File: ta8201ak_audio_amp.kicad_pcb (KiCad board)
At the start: 2 copper layers, 42.3 x 35.4 mm, 20 parts, among them J1 Conn_01x01_Pin, J2 Conn_01x01_Pin, J3 Conn_01x01_Pin, J4 Conn_01x01_Pin, J5 Conn_01x01_Pin, U1 TA8201AK

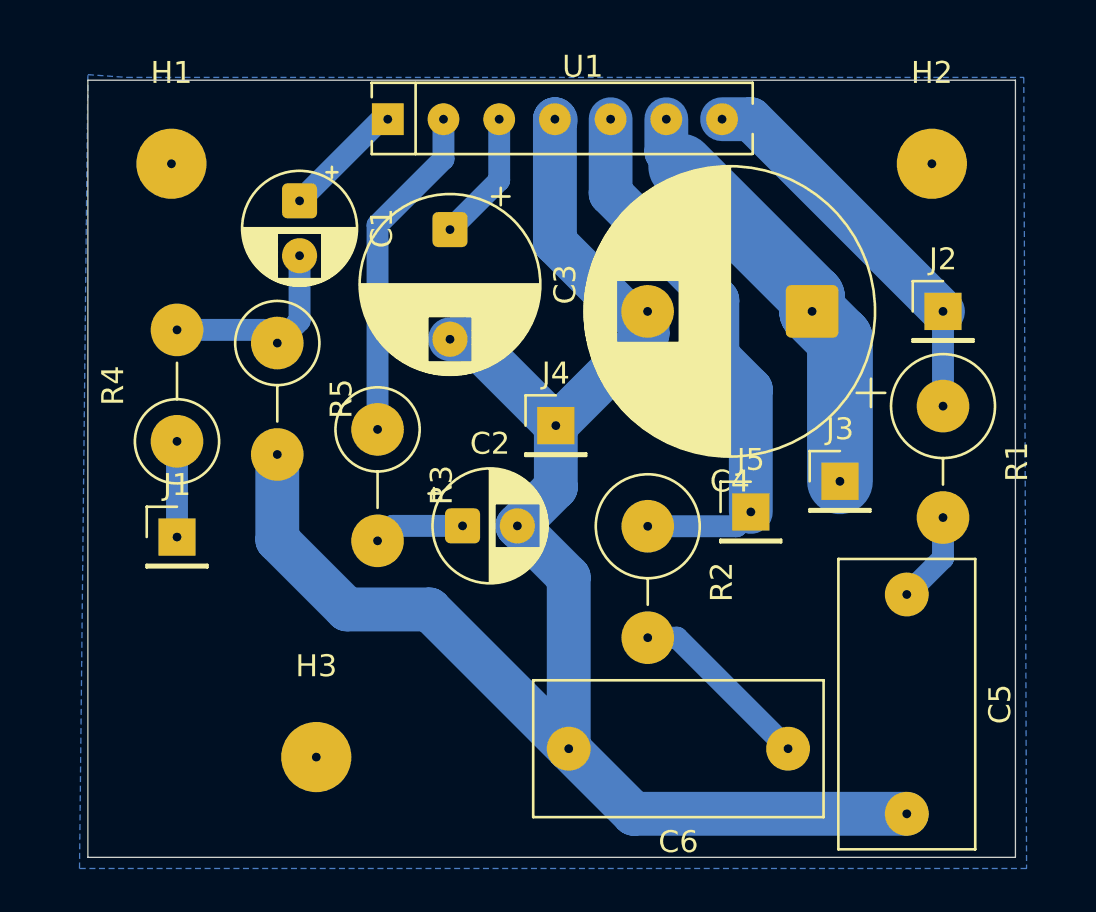
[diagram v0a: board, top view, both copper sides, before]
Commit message: 配置と配線を修正
配線の修正
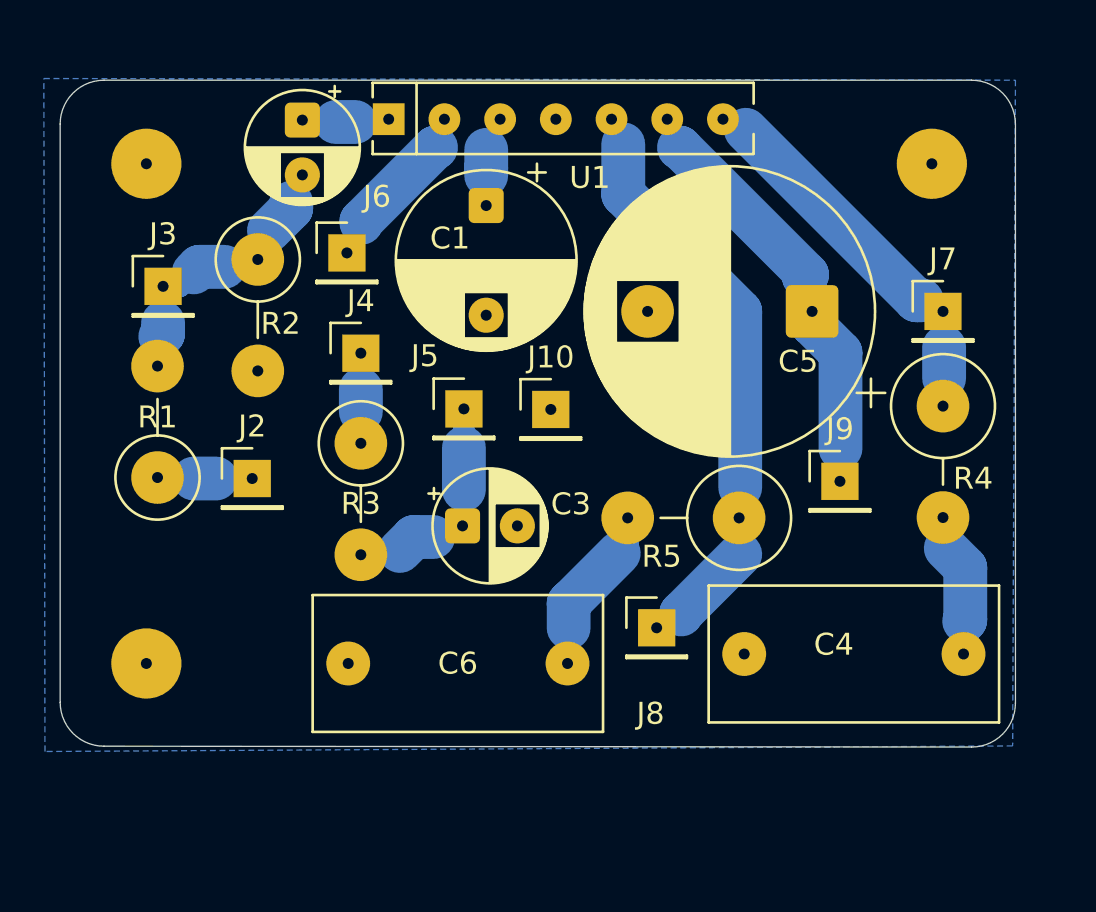
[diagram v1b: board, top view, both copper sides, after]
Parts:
- removed J1: Conn_01x01_Pin, Connector_PinHeader_2.54mm:PinHeader_1x01_P2.54mm_Vertical
- removed the R1 at (189.7, 68.1)
- added J2: SW1_1, Connector_PinHeader_2.54mm:PinHeader_1x01_P2.54mm_Vertical, F.Cu at (158.2, 71.4)
- added J3: SW1_2, Connector_PinHeader_2.54mm:PinHeader_1x01_P2.54mm_Vertical, F.Cu at (154.2, 62.6)
- added J4: SW2_2, Connector_PinHeader_2.54mm:PinHeader_1x01_P2.54mm_Vertical, F.Cu at (163.2, 65.7)
- added J5: SW2_3, Connector_PinHeader_2.54mm:PinHeader_1x01_P2.54mm_Vertical, F.Cu at (167.9, 68.2)
- added J6: SW2_1, Connector_PinHeader_2.54mm:PinHeader_1x01_P2.54mm_Vertical, F.Cu at (162.6, 61.1)
- added R4: 2.2, Resistor_THT:R_Axial_DIN0414_L11.9mm_D4.5mm_P5.08mm_Vertical, F.Cu at (189.7, 68.1)
- C1: renamed from C3; value 220uF -> 220u
- C3: renamed from C2; value 47uF -> 47u
- C4: renamed from C5; value 0.15uF -> 0.15u
- C6: value 0.15uF -> 0.15u
- J10: renamed from J4; value Conn_01x01_Pin -> Gnd
- J7: renamed from J2; value Conn_01x01_Pin -> Out1
- J8: renamed from J5; value Conn_01x01_Pin -> Out2
- J9: renamed from J3; value Conn_01x01_Pin -> Vcc
- R1: renamed from R4; value 39kΩ -> 39k
- R2: renamed from R5; value 10kΩ -> 10k
- U1: value TA8201AK -> ~
- moved C6 10.8 mm to (172.6, 79.8)
- moved H3 8.84 mm to (153.4, 79.8)
- moved J8 6.81 mm to (176.7, 78.2)
- moved R5 4.18 mm to (180.4, 73.2), turned to 180 degrees
- moved R2 3.91 mm to (158.5, 61.4)
- moved C4 3.75 mm to (190.7, 79.4), turned to 180 degrees
- moved C2 3.69 mm to (160.5, 55.0)
- moved C1 1.98 mm to (168.9, 58.9)
- moved R1 1.88 mm to (153.9, 71.3)
- moved H1 1.14 mm to (153.4, 57.0)
- moved R3 0.99 mm to (163.2, 69.8)
- moved J10 0.77 mm to (171.9, 68.2)
- renumbered C1 to C2, C4 to C5, R2 to R5
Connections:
- R3 pad 1: Net-(U1-NF) -> Net-(J4-Pin_1)
- U1 pad 2: Net-(U1-NF) -> Net-(J6-Pin_1)
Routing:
- net GND: track 78.8 -> 0.00 mm
- net Net-(U1-NF): track 15.4 -> 0.00 mm
- net Net-(J6-Pin_1): track 0.00 -> 4.87 mm
- net Net-(U1-R.F): track 5.96 -> 1.17 mm
- net Net-(J7-Pin_1): track 18.0 -> 14.1 mm
- net Net-(J5-Pin_1): track 4.16 -> 7.36 mm
- net Net-(U1-IN): track 5.56 -> 2.45 mm
- net VCC: track 19.8 -> 16.9 mm
- net Net-(C4-Pad1): track 4.19 -> 6.68 mm
- net Net-(J4-Pin_1): track 0.00 -> 2.46 mm
- net Net-(J2-Pin_1): track 4.36 -> 2.69 mm
- net Net-(J3-Pin_1): track 9.22 -> 8.47 mm
- net Net-(C6-Pad1): track 8.49 -> 7.77 mm
- net Net-(J8-Pin_1): track 25.5 -> 25.0 mm
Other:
- board size 42.3 x 35.4 mm -> 43.6 x 30.4 mm

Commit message: 仕切り直す
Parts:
- removed the J2 at (158.2, 71.4)
- removed the J3 at (154.2, 62.6)
- removed the J4 at (163.2, 65.7)
- removed the J5 at (167.9, 68.2)
- removed J6: SW2_1, Connector_PinHeader_2.54mm:PinHeader_1x01_P2.54mm_Vertical
- added J1: IN, Connector_PinHeader_2.54mm:PinHeader_1x01_P2.54mm_Vertical, F.Cu at (158.5, 71.4)
- C2: renamed from C3; value 47u -> 47uF
- C3: renamed from C1; value 220u -> 220uF
- C5: renamed from C4; value 0.15u -> 0.15uF
- C6: value 0.15u -> 0.15uF
- R4: renamed from R1; value 39k -> 39kΩ
- R5: renamed from R2; value 10k -> 10kΩ
- renumbered C2 to C1, C5 to C4, J7 to J2, J9 to J3, J10 to J4, J8 to J5, R4 to R1, R5 to R2
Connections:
- R3 pad 1: Net-(J4-Pin_1) -> Net-(U1-NF)
- U1 pad 2: Net-(J6-Pin_1) -> Net-(U1-NF)
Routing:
- net Net-(U1-NF): track 0.00 -> 14.9 mm
- net Net-(J6-Pin_1): track 4.87 -> 0.00 mm
- net Net-(C2-Pad1): track 7.36 -> 3.67 mm
- net Net-(J4-Pin_1): track 2.46 -> 0.00 mm

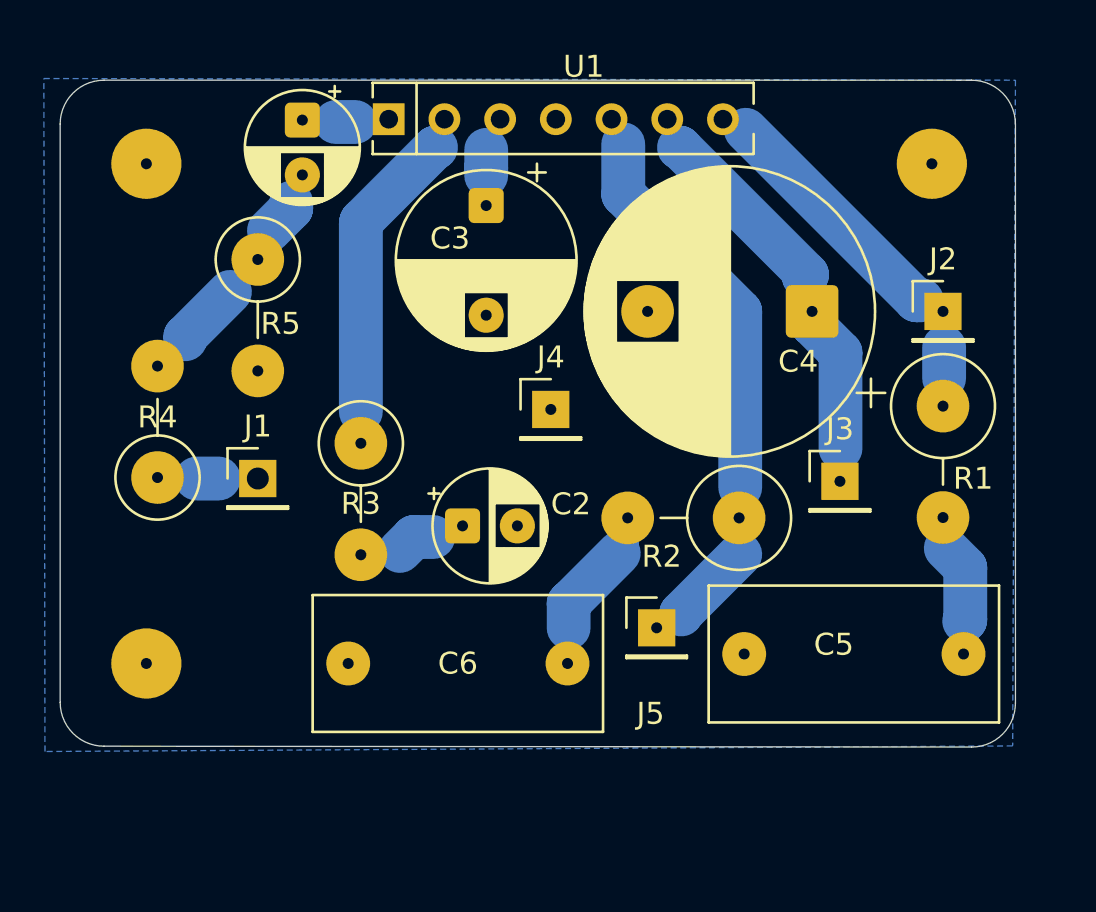
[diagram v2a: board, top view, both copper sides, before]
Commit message: エレキギター向けに抵抗やコンデンサを変更
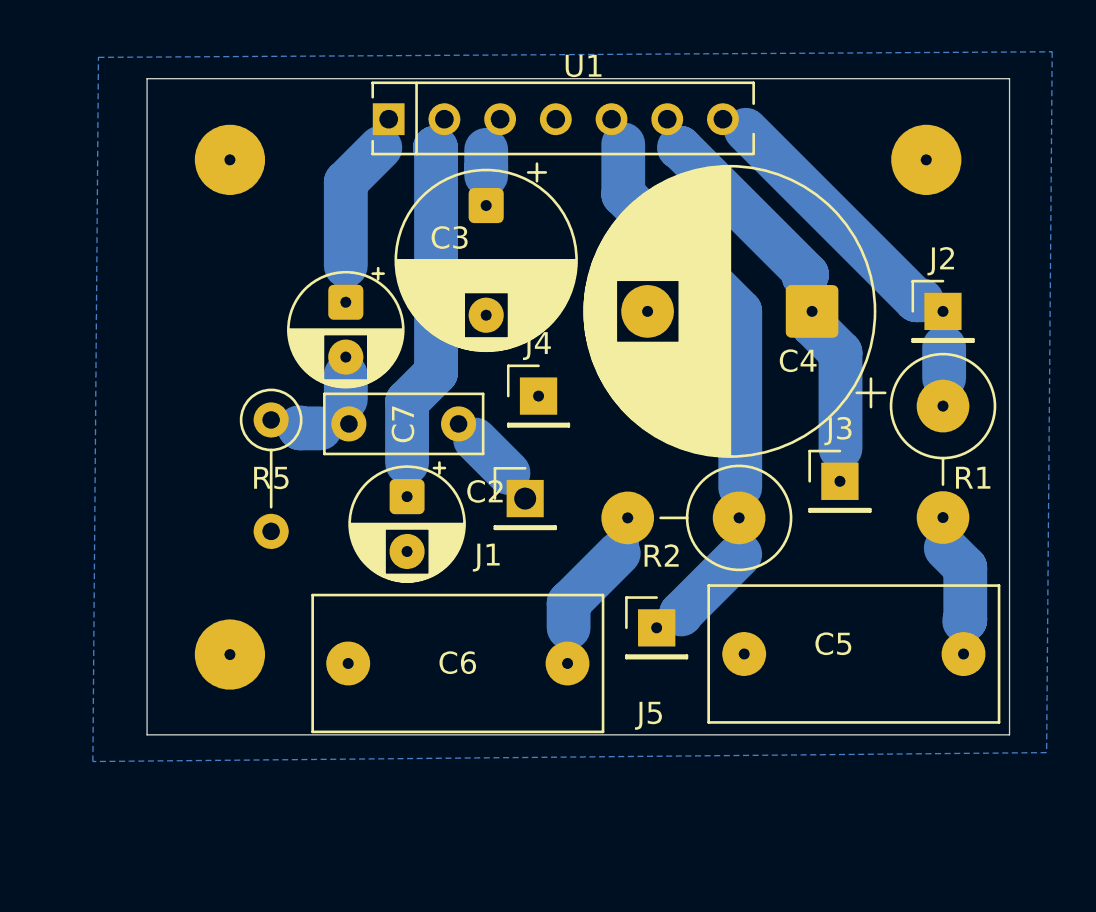
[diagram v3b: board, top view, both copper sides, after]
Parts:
- removed R3: 620, Resistor_THT:R_Axial_DIN0411_L9.9mm_D3.6mm_P5.08mm_Vertical
- removed R4: 39kΩ, Resistor_THT:R_Axial_DIN0411_L9.9mm_D3.6mm_P5.08mm_Vertical
- added C7: 0.022u, Capacitor_THT:C_Rect_L7.0mm_W2.5mm_P5.00mm, F.Cu at (167.7, 68.9)
- C1: value 4.7uF -> 4.7u
- C2: value 47uF -> 47u
- C3: value 220uF -> 220u
- C4: value 1000uF -> 1000u
- C5, C6: value 0.15uF -> 0.15u
- R5: value 10kΩ -> 1M; footprint Resistor_THT:R_Axial_DIN0411_L9.9mm_D3.6mm_P5.08mm_Vertical -> Resistor_THT:R_Axial_DIN0207_L6.3mm_D2.5mm_P5.08mm_Vertical
- moved J1 12.2 mm to (170.7, 72.3)
- moved C1 8.54 mm to (162.5, 63.3)
- moved R5 7.34 mm to (159.1, 68.7)
- moved H3 3.83 mm to (157.2, 79.4)
- moved H1 3.81 mm to (157.2, 56.8)
- moved C2 2.86 mm to (165.3, 72.2), turned to -90 degrees
- moved J4 0.83 mm to (171.3, 67.6)
- moved H2 0.31 mm to (189.0, 56.8)
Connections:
- C2 pad 1: Net-(C2-Pad1) -> Net-(U1-NF)
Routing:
- net Net-(U1-IN): track 2.45 -> 7.70 mm
- net Net-(C1-Pad2): track 7.99 -> 2.97 mm
- net Net-(C2-Pad1): track 3.67 -> 0.00 mm
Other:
- board size 43.6 x 30.4 mm -> 39.3 x 29.9 mm

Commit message: 利得制限の抵抗は外した アッテネーターの合成抵抗をエレキギター向けに1Mに近づけた 高音補正用のセラミックコンデンサとボリュームを追加
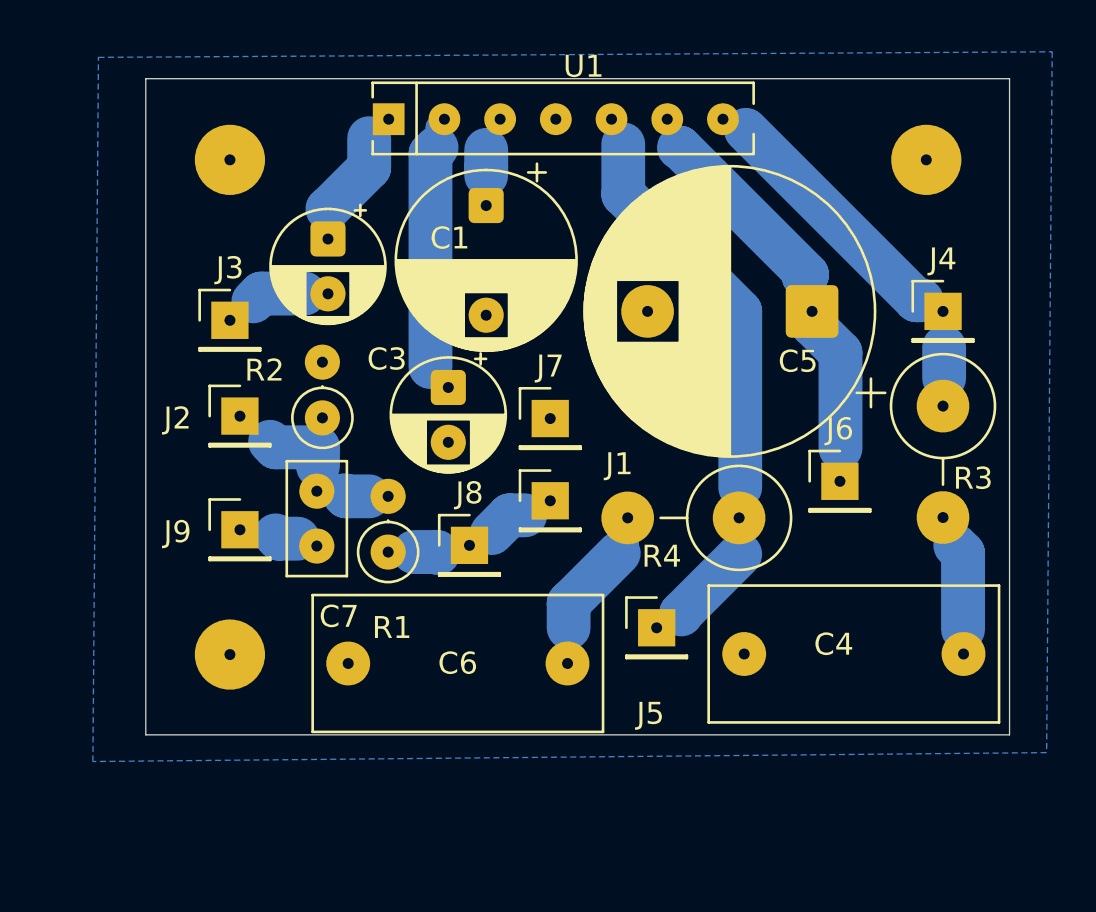
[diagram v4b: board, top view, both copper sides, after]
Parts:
- removed the C2 at (165.3, 72.2)
- added C3: 47u, Capacitor_THT:CP_Radial_D5.0mm_P2.50mm, F.Cu at (167.2, 67.2)
- added J2: RV1_3, Connector_PinHeader_2.54mm:PinHeader_1x01_P2.54mm_Vertical, F.Cu at (157.7, 68.5)
- added J3: RV1_2, Connector_PinHeader_2.54mm:PinHeader_1x01_P2.54mm_Vertical, F.Cu at (157.2, 64.2)
- added J8: SW1_1, Connector_PinHeader_2.54mm:PinHeader_1x01_P2.54mm_Vertical, F.Cu at (168.1, 74.4)
- added J9: SW1_2, Connector_PinHeader_2.54mm:PinHeader_1x01_P2.54mm_Vertical, F.Cu at (157.7, 73.7)
- added R1: 200k, Resistor_THT:R_Axial_DIN0207_L6.3mm_D2.5mm_P2.54mm_Vertical, F.Cu at (164.4, 74.7)
- C7: value 0.022u -> 100p; footprint Capacitor_THT:C_Rect_L7.0mm_W2.5mm_P5.00mm -> Capacitor_THT:C_Disc_D5.0mm_W2.5mm_P2.50mm
- R2: renamed from R5; value 1M -> 820k; footprint Resistor_THT:R_Axial_DIN0207_L6.3mm_D2.5mm_P5.08mm_Vertical -> Resistor_THT:R_Axial_DIN0207_L6.3mm_D2.5mm_P2.54mm_Vertical
- moved C7 8.53 mm to (161.2, 74.5), turned to 90 degrees
- moved C2 3.00 mm to (161.7, 60.5)
- moved R2 2.34 mm to (161.4, 68.6), turned to 90 degrees
- moved J7 1.16 mm to (171.8, 68.6)
- moved J1 1.15 mm to (171.8, 72.4)
- turned H3 to 90 degrees
- renumbered C3 to C1, C1 to C2, C5 to C4, C4 to C5, J2 to J4, J3 to J6, J4 to J7, R1 to R3, R2 to R4
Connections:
- C2 pad 2: Net-(C1-Pad2) -> Net-(J3-Pin_1)
- C7 pad 1: Net-(J1-Pin_1) -> Net-(J9-Pin_1)
- C7 pad 2: Net-(C1-Pad2) -> Net-(J2-Pin_1)
- R2 pad 1: Net-(C1-Pad2) -> Net-(J2-Pin_1)
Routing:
- net Net-(J2-Pin_1): track 0.00 -> 6.31 mm
- net Net-(J3-Pin_1): track 0.00 -> 3.56 mm
- net Net-(U1-NF): track 15.0 -> 11.6 mm
- net Net-(C1-Pad2): track 2.97 -> 0.00 mm
- net Net-(U1-IN): track 7.70 -> 5.41 mm
- net Net-(J1-Pin_1): track 3.20 -> 5.42 mm
- net Net-(J9-Pin_1): track 0.00 -> 2.08 mm
- net Net-(C4-Pad1): track 6.68 -> 5.11 mm
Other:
- board size 39.3 x 29.9 mm -> 39.4 x 29.9 mm

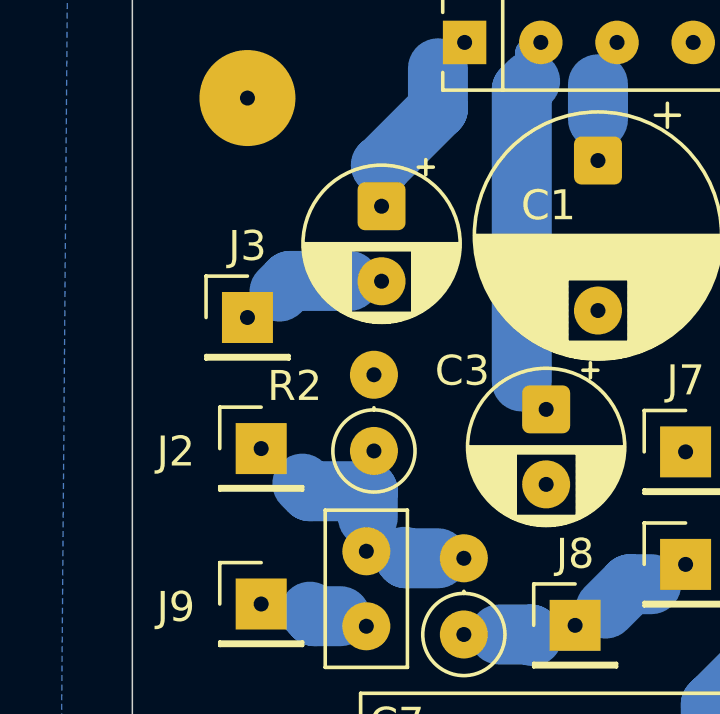
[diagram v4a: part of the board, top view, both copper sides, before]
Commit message: GNDが細い一点で繋がっていたので少しでも太くなるよう配置修正
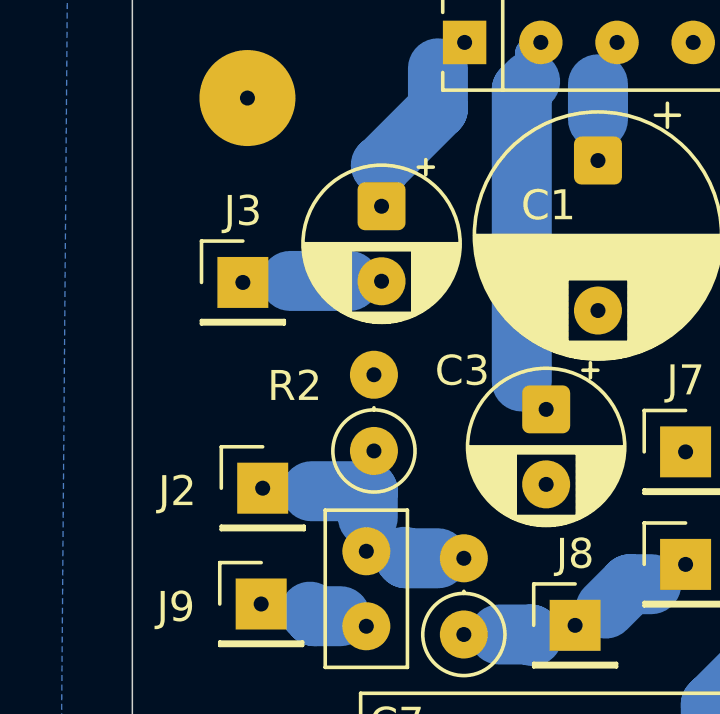
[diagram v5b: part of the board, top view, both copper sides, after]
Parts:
- moved J2 1.32 mm to (157.7, 69.8)
- moved J3 1.18 mm to (157.1, 63.0)
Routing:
- net Net-(J3-Pin_1): track 3.56 -> 3.05 mm
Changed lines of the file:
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@@
 	(footprint "Connector_PinHeader_2.54mm:PinHeader_1x01_P2.54mm_Vertical"
 		(layer "F.Cu")
-		(at 157.226 64.1604)
+		(at 157.0736 62.992)
 		(descr "Through hole straight pin header, 1x01, 2.54mm pitch, single row")
 		(tags "Through hole pin header THT 1x01 2.54mm single row")
@@
 	(footprint "Connector_PinHeader_2.54mm:PinHeader_1x01_P2.54mm_Vertical"
 		(layer "F.Cu")
-		(at 157.6832 68.5292)
+		(at 157.734 69.85)
 		(descr "Through hole straight pin header, 1x01, 2.54mm pitch, single row")
 		(tags "Through hole pin header THT 1x01 2.54mm single row")
@@
 	)
 	(segment
-		(start 159.3088 69.9516)
-		(end 159.0548 69.6976)
-		(width 2)
-		(layer "B.Cu")
-		(net 5)
-	)
-	(segment
 		(start 163.576 72.1868)
 		(end 162.5092 72.1868)
@@
 	)
 	(segment
-		(start 161.1884 70.866)
-		(end 161.2392 70.8152)
-		(width 1)
-		(layer "B.Cu")
-		(net 5)
-	)
-	(segment
 		(start 164.4396 72.1868)
 		(end 163.576 72.1868)
@@
 	)
 	(segment
-		(start 161.2392 69.9516)
-		(end 159.3088 69.9516)
+		(start 162.5092 72.1868)
+		(end 162.4584 72.136)
 		(width 2)
 		(layer "B.Cu")
@@
 	)
 	(segment
-		(start 162.5092 72.1868)
-		(end 162.4584 72.136)
+		(start 161.2392 69.9516)
+		(end 159.3596 69.9516)
 		(width 2)
 		(layer "B.Cu")
@@
 		(layer "B.Cu")
 		(net 10)
-	)
-	(segment
-		(start 158.6484 62.9412)
-		(end 158.2928 63.2968)
-		(width 2)
-		(layer "B.Cu")
-		(net 10)
